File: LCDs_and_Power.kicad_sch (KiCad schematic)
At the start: 37 parts, among them CN1 LIPO BATTERY, U11 BQ24295, U3 AP3031KTR-G1 - ref 200mV, U6 AP2112

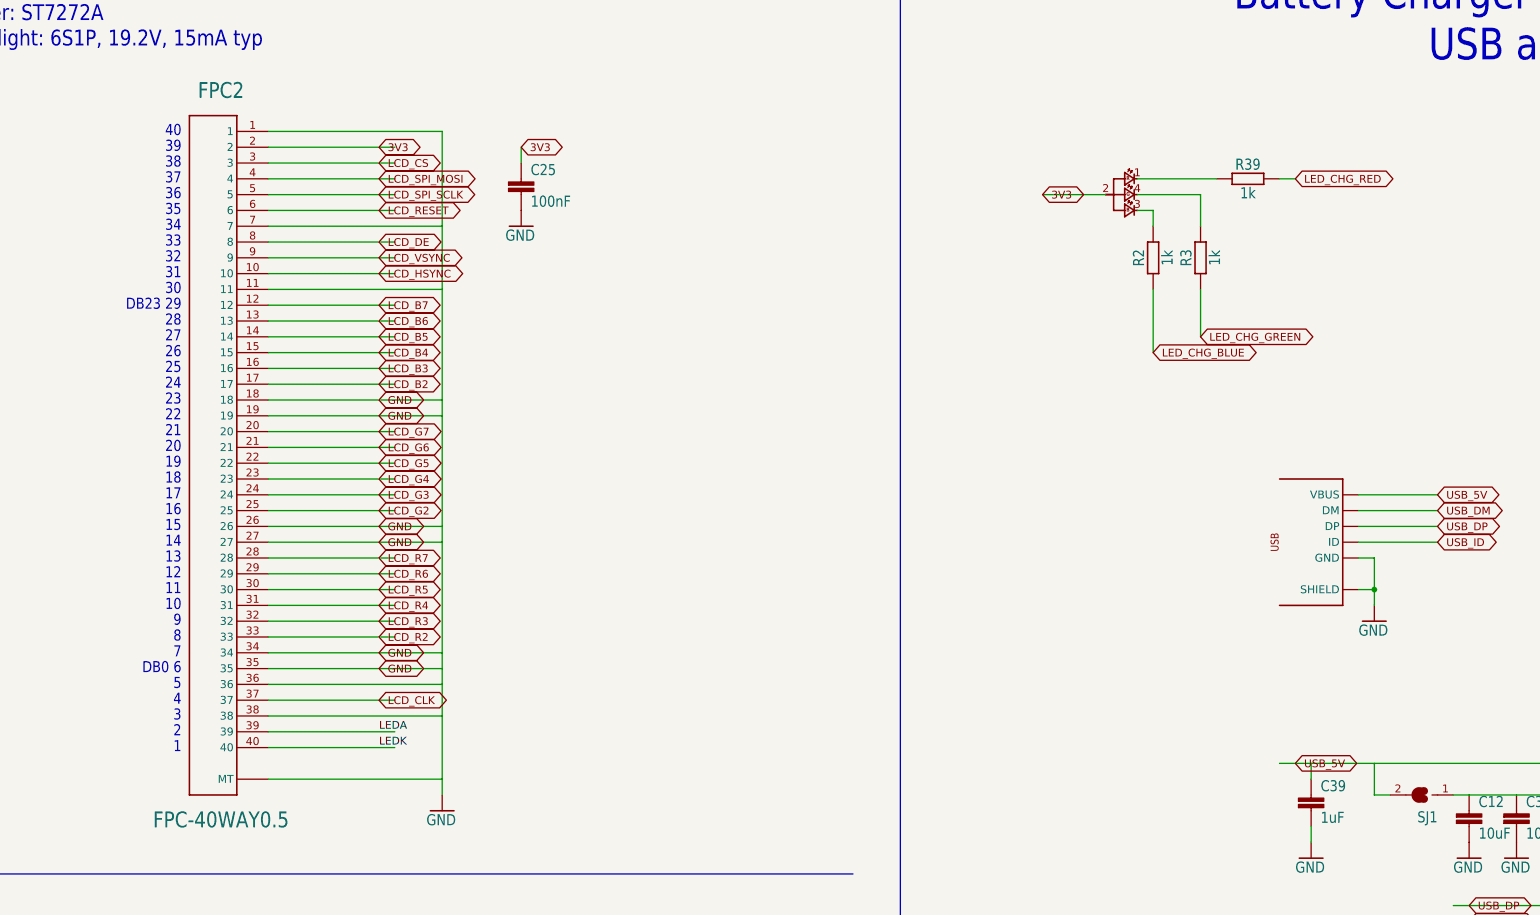
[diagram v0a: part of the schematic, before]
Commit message: Use kicad footprints for resistors/capacitors
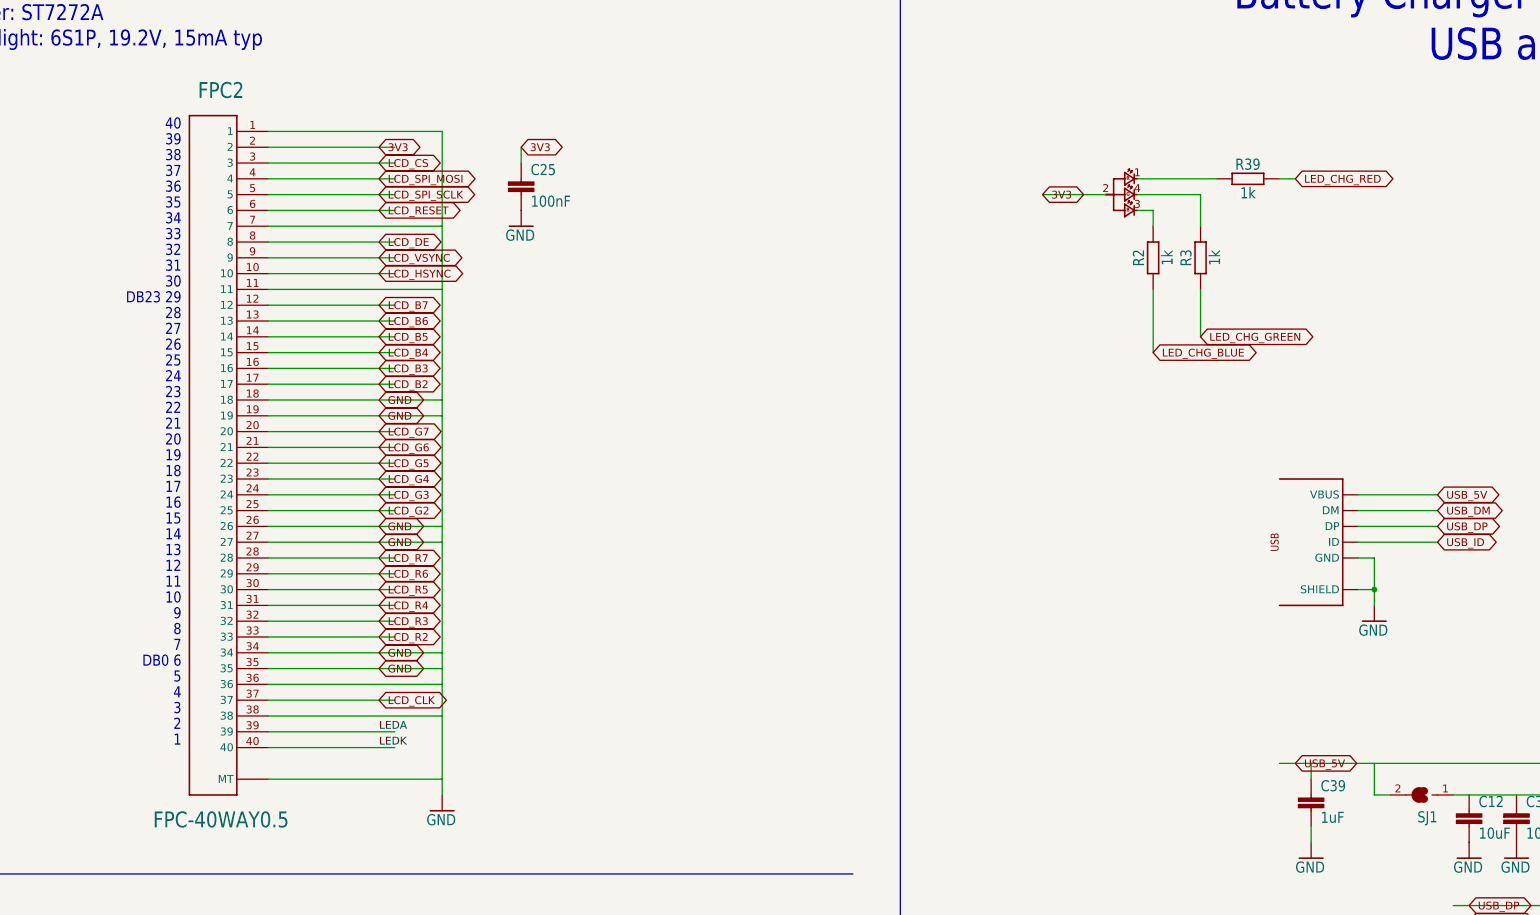
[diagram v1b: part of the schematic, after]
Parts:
- BAT_THERM0: footprint 32blit:0402@1 -> Resistor_SMD:R_0402_1005Metric
- C12, C37, C41, C42, C43, C44: footprint 32blit:C0805 -> Capacitor_SMD:C_0805_2012Metric
- C21, C25, C40: footprint 32blit:C0402K -> Capacitor_SMD:C_0402_1005Metric
- C22, C27, C28, C34, C39: footprint 32blit:C0603 -> Capacitor_SMD:C_0603_1608Metric
- R10, R11, R2, R3, R36, R37, R39, R40, R6, R7, R8: footprint 32blit:R0603 -> Resistor_SMD:R_0603_1608Metric

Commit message: More footprint replacements
This involved some adjusting for pad sizes
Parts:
- CN1: footprint 32blit:JST-PH-2-SMT-RA -> Connector_JST:JST_PH_S2B-PH-SM4-TB_1x02-1MP_P2.00mm_Horizontal
- L1: footprint 32blit:NRS5030 -> Inductor_SMD:L_Taiyo-Yuden_NR-50xx
- L2: footprint 32blit:NR4018 -> Inductor_SMD:L_Taiyo-Yuden_NR-40xx
- U3: footprint 32blit:SOT23-6L -> Package_TO_SOT_SMD:SOT-23-6
- U6: footprint 32blit:SOT-23-5 -> Package_TO_SOT_SMD:SOT-23-5
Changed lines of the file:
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@@
       (effects (font (size 1.27 1.0795)) (justify left bottom))
     )
-    (property "Footprint" "32blit:NRS5030" (at 347.98 162.56 0)
+    (property "Footprint" "Inductor_SMD:L_Taiyo-Yuden_NR-50xx" (at 347.98 162.56 0)
       (effects (font (size 1.27 1.27)) hide)
     )
@@
       (effects (font (size 1.27 1.0795)) (justify left bottom))
     )
-    (property "Footprint" "32blit:NR4018" (at 104.14 218.44 0)
+    (property "Footprint" "Inductor_SMD:L_Taiyo-Yuden_NR-40xx" (at 104.14 218.44 0)
       (effects (font (size 1.27 1.27)) hide)
     )
@@
       (effects (font (size 1.778 1.5113)) (justify left bottom))
     )
-    (property "Footprint" "32blit:JST-PH-2-SMT-RA" (at 297.18 127 0)
+    (property "Footprint" "Connector_JST:JST_PH_S2B-PH-SM4-TB_1x02-1MP_P2.00mm_Horizontal" (at 297.18 127 0)
       (effects (font (size 1.27 1.27)) hide)
     )
@@
       (effects (font (size 2.032 1.7272)) (justify left bottom))
     )
-    (property "Footprint" "32blit:SOT23-6L" (at 99.06 236.22 0)
+    (property "Footprint" "Package_TO_SOT_SMD:SOT-23-6" (at 99.06 236.22 0)
       (effects (font (size 1.27 1.27)) hide)
     )
@@
       (effects (font (size 1.778 1.5113)) (justify left bottom))
     )
-    (property "Footprint" "32blit:SOT-23-5" (at 358.14 71.12 0)
-      (effects (font (size 1.27 1.27)) hide)
-    )
+    (property "Footprint" "Package_TO_SOT_SMD:SOT-23-5" (at 358.14 71.12 0)
+      (effects (font (size 1.27 1.27)) hide)
+    )

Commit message: Remove custom pimoroni frame
Makes the sch a bit hard to work with and recreating it in the .kicad_wks seems difficult
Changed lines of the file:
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@@
-    )
-  )
-  (symbol (lib_id "32blit-eagle-import:DINA3_PIM_L") (at 17.78 281.94 0) (unit 1)
-    (in_bom yes) (on_board yes) (dnp no)
-    (property "Reference" "#FRAME5" (at 17.78 281.94 0)
-      (effects (font (size 1.27 1.27)) hide)
-    )
-    (property "Value" "DINA3_PIM_L" (at 17.78 281.94 0)
-      (effects (font (size 1.27 1.27)) hide)
-    )
-    (property "Footprint" "" (at 17.78 281.94 0)
-      (effects (font (size 1.27 1.27)) hide)
-    )
-    (property "Datasheet" "" (at 17.78 281.94 0)
-      (effects (font (size 1.27 1.27)) hide)
-    )
-    (instances
-      (project "32blit"
-        (path "/5e392b0a-93d8-4fe3-995e-b41db5e69183/7219dd04-59a8-484d-b130-3c1a1283275c"
-          (reference "#FRAME5") (unit 1)
-        )
-      )
     )
   )

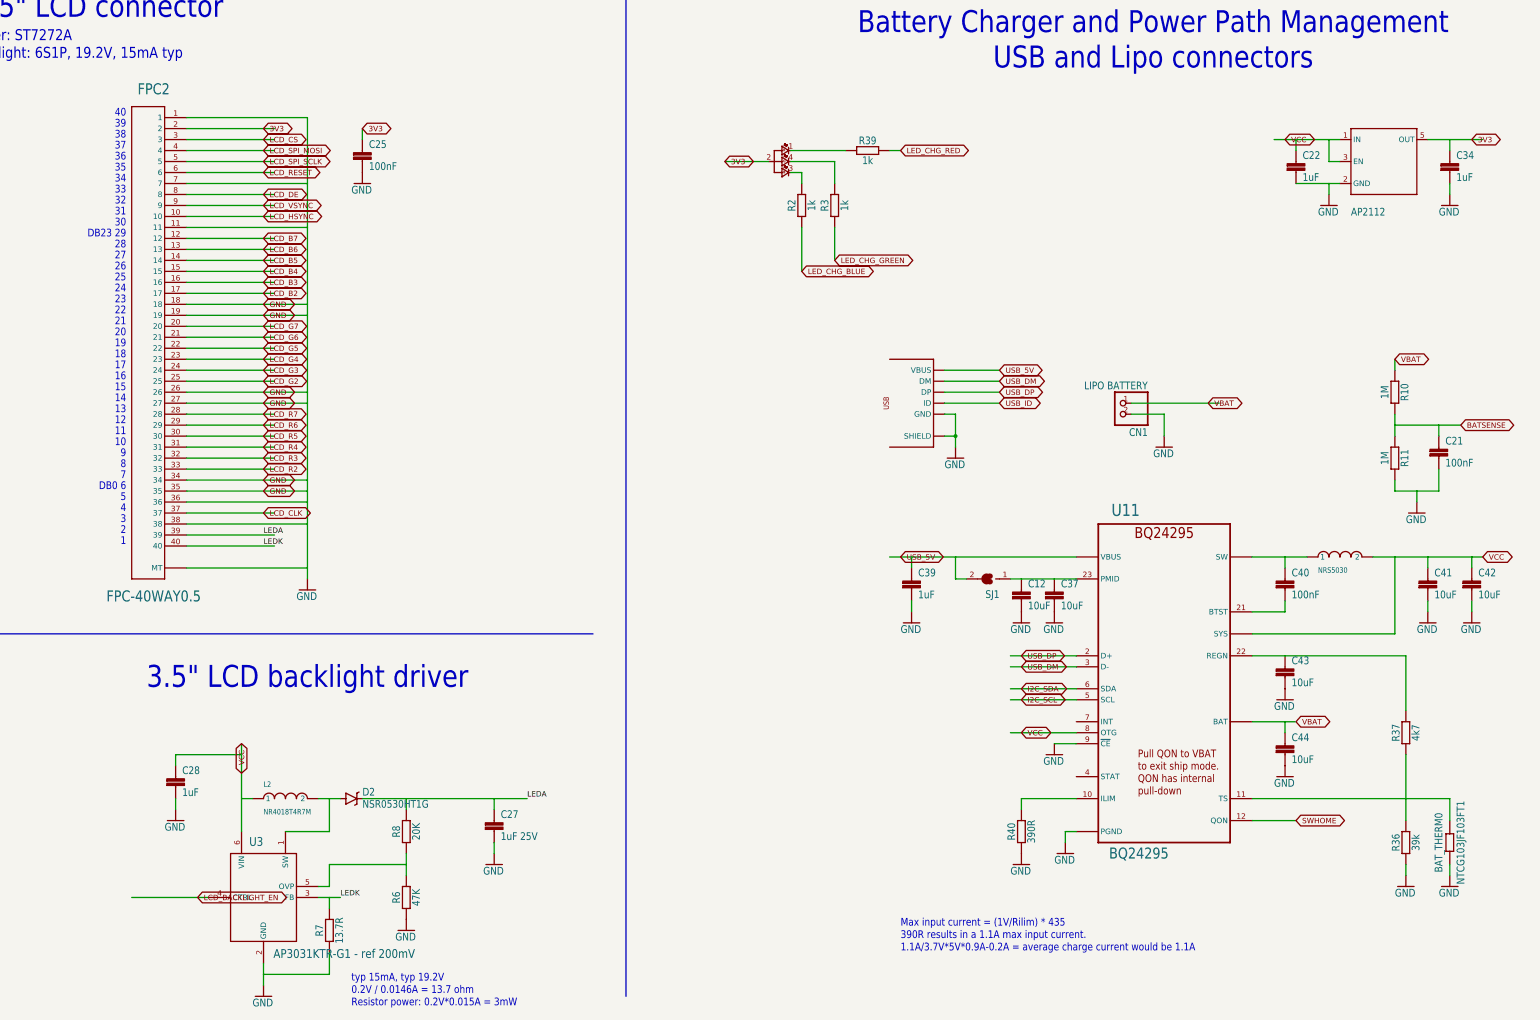
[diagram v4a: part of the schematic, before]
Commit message: Giant schematic rework
Use as many kicad symbols as possiblem, adjust remaining imported symbols to make ERC happy and adjust some footprints for the new symbols
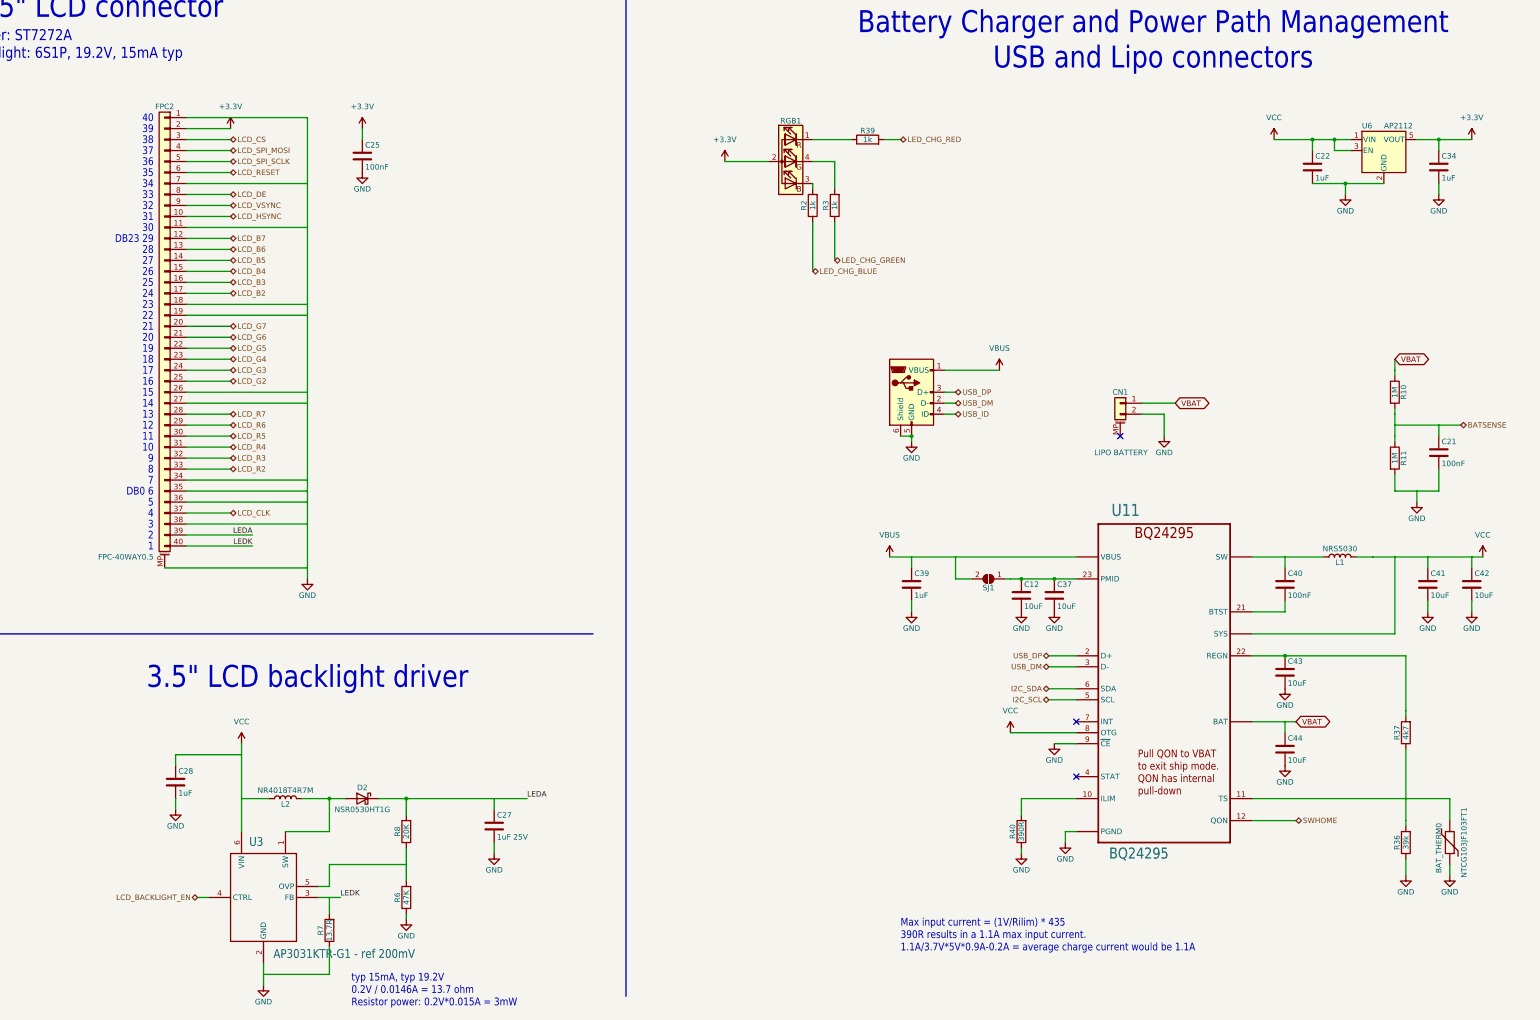
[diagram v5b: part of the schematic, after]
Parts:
- BAT_THERM0: symbol 32blit-eagle-import:RESISTOR.0402 -> Device:Thermistor
- C12, C37, C41, C42, C43, C44: symbol 32blit-eagle-import:C-EUC0805 -> Device:C
- C21, C25, C40: symbol 32blit-eagle-import:rcl_C-EUC0402K -> Device:C
- C22, C27, C28, C34, C39: symbol 32blit-eagle-import:C-EUC0603 -> Device:C
- CN1: symbol 32blit-eagle-import:JST_2PIN-SMT-RA -> Connector_Generic_MountingPin:Conn_01x02_MountingPin
- D2: symbol 32blit-eagle-import:NSR0530HT1G -> Device:D_Schottky
- FPC2: symbol 32blit-eagle-import:FPC-40WAY0.5 -> Connector_Generic_MountingPin:Conn_01x40_MountingPin
- L1: symbol 32blit-eagle-import:NRS5030 -> Device:L
- L2: symbol 32blit-eagle-import:NR4018T4R7M -> Device:L
- R10, R11, R2, R3, R36, R37, R39, R40, R6, R7, R8: symbol 32blit-eagle-import:R-EU_R0603 -> Device:R
- RGB1: symbol 32blit-eagle-import:LED_RGB_4P6028_REVERSE -> Device:LED_RABG
- SJ1: symbol 32blit-eagle-import:SOLDERJUMPER -> Jumper:SolderJumper_2_Open
- U$3: symbol 32blit-eagle-import:USBMICROB -> Connector:USB_B_Micro
- U6: symbol 32blit-eagle-import:AP2112 -> Regulator_Linear:AP2112K-3.3
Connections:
- net GND: now also FPC2.MP (MountPin), U$3.5 (GND), U$3.6 (Shield); no longer FPC2.MT1 (MT), FPC2.MT2 (MT), U$3.GND, U$3.SH1 (SHIELD), U$3.SH2 (SHIELD), U$3.SH3 (SHIELD), U$3.SH4 (SHIELD), U$3.SH5 (SHIELD), U$3.SH6 (SHIELD), U$3.SH7 (SHIELD), U$3.SH8 (SHIELD)
- net LEDA: now also D2.1 (K); no longer D2.C
- net USB_DM: now also U$3.2 (D-); no longer U$3.DM
- net USB_DP: now also U$3.3 (D+); no longer U$3.DP
- net USB_ID: now also U$3.4 (ID); no longer U$3.ID
- net at L2.2, U3.1 (SW): now also D2.2 (A); no longer D2.A
- net 3V3 renamed +3.3V
- net USB_5V renamed VBUS
- net VBUS: now also U$3.1 (VBUS); no longer U$3.VBUS
- no-connect marks 0 -> 3
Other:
- moved on the sheet: FPC2
